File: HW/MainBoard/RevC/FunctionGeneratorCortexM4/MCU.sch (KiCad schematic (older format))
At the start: 13 parts, among them J3 Conn_02x06_Odd_Even, J4 Conn_01x06, J6 Conn_02x04_Odd_Even, J7 Conn_02x07_Odd_Even, U2 TS5A3357, U6 STM32G474RET

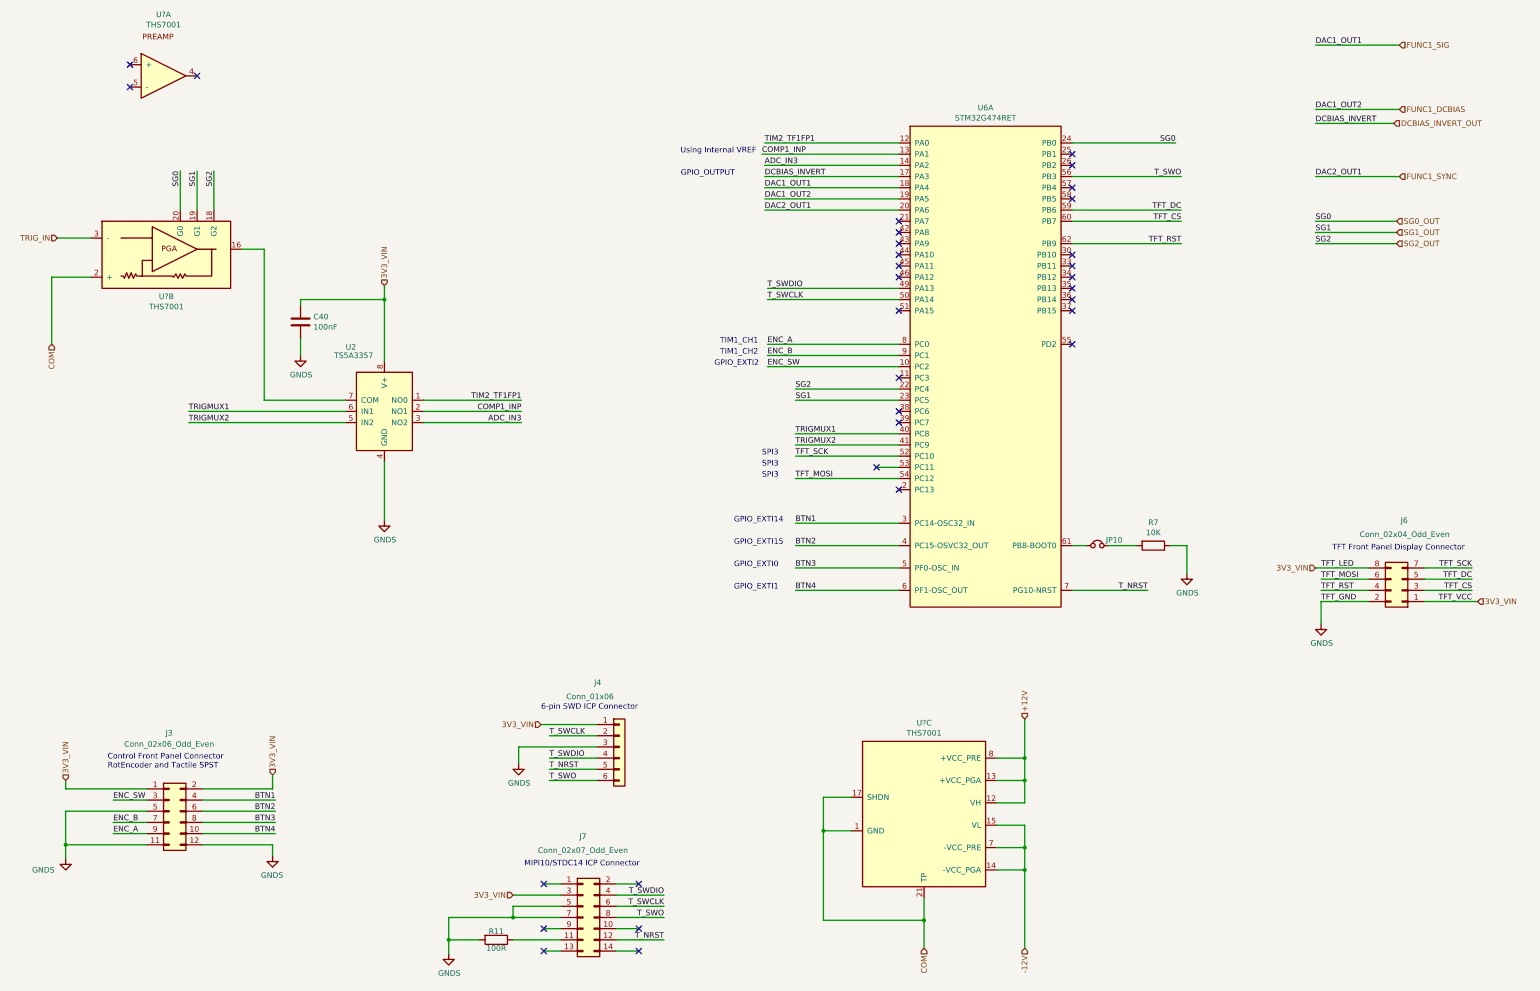
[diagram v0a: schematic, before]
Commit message: Updated MainBoard RevC
- Block diagram and connections completed on schematic
- Need to check MCU pin availability
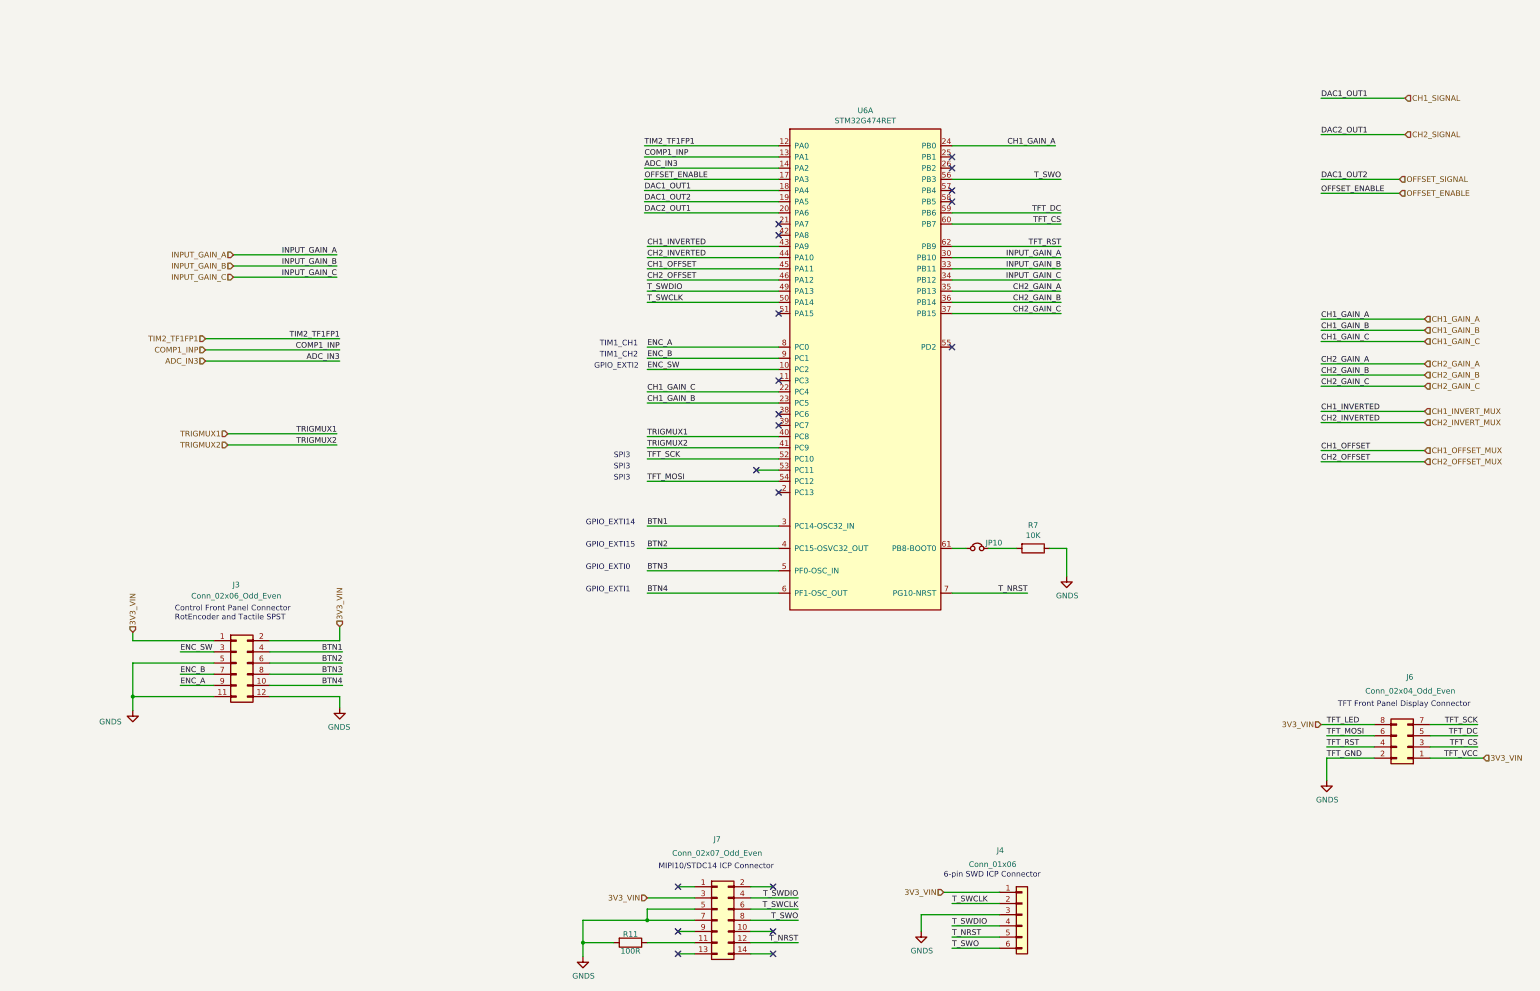
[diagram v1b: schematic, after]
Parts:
- removed C40: 100nF, Capacitor_SMD:C_0603_1608Metric_Pad1.05x0.95mm_HandSolder, symbol Device:C
- removed U2: TS5A3357, Package_SO:VSSOP-8_2.4x2.1mm_P0.5mm, symbol TS5A3357:TS5A3357
- removed U? (x3): THS7001, Package_SO:TSSOP-20_4.4x6.5mm_P0.65mm, symbol PGA:THS7001
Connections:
- net INPUT_GAIN_A: now reaches U6.30 (PB10)
- net INPUT_GAIN_B: now reaches U6.33 (PB11)
- net INPUT_GAIN_C: now reaches U6.34 (PB12)
- net CH2_GAIN_A: now reaches U6.35 (PB13)
- net CH2_GAIN_B: now reaches U6.36 (PB14)
- net CH2_GAIN_C: now reaches U6.37 (PB15)
- net CH1_INVERT_MUX: now reaches U6.43 (PA9)
- net CH2_INVERT_MUX: now reaches U6.44 (PA10)
- net CH1_OFFSET_MUX: now reaches U6.45 (PA11)
- net CH2_OFFSET_MUX: now reaches U6.46 (PA12)
- net DCBIAS_INVERT_OUT renamed OFFSET_ENABLE
- net FUNC1_DCBIAS renamed OFFSET_SIGNAL
- net FUNC1_SIG renamed CH1_SIGNAL
- net FUNC1_SYNC renamed CH2_SIGNAL
- net SG0_OUT renamed CH1_GAIN_A
- net SG1_OUT renamed CH1_GAIN_B
- net SG2_OUT renamed CH1_GAIN_C
- no-connect marks 32 -> 19
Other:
- note removed: "GPIO_OUTPUT"
- note removed: "Using Internal VREF"
- moved on the sheet: J3, J4, J6, J7, JP10, R11, R7, U6A
